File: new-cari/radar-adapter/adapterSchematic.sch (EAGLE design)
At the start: 25 parts, among them J3 JST-XH-03-PIN-LONG-PAD, J4 JST-XH-03-PIN-LONG-PAD, J5 AVR_SPI_PROG_3X2PTH, J6 UX60-MB-5S8, U1 ATMEGA32U4-AU, X1 TSX-3225 16.0000MF18X-AC0

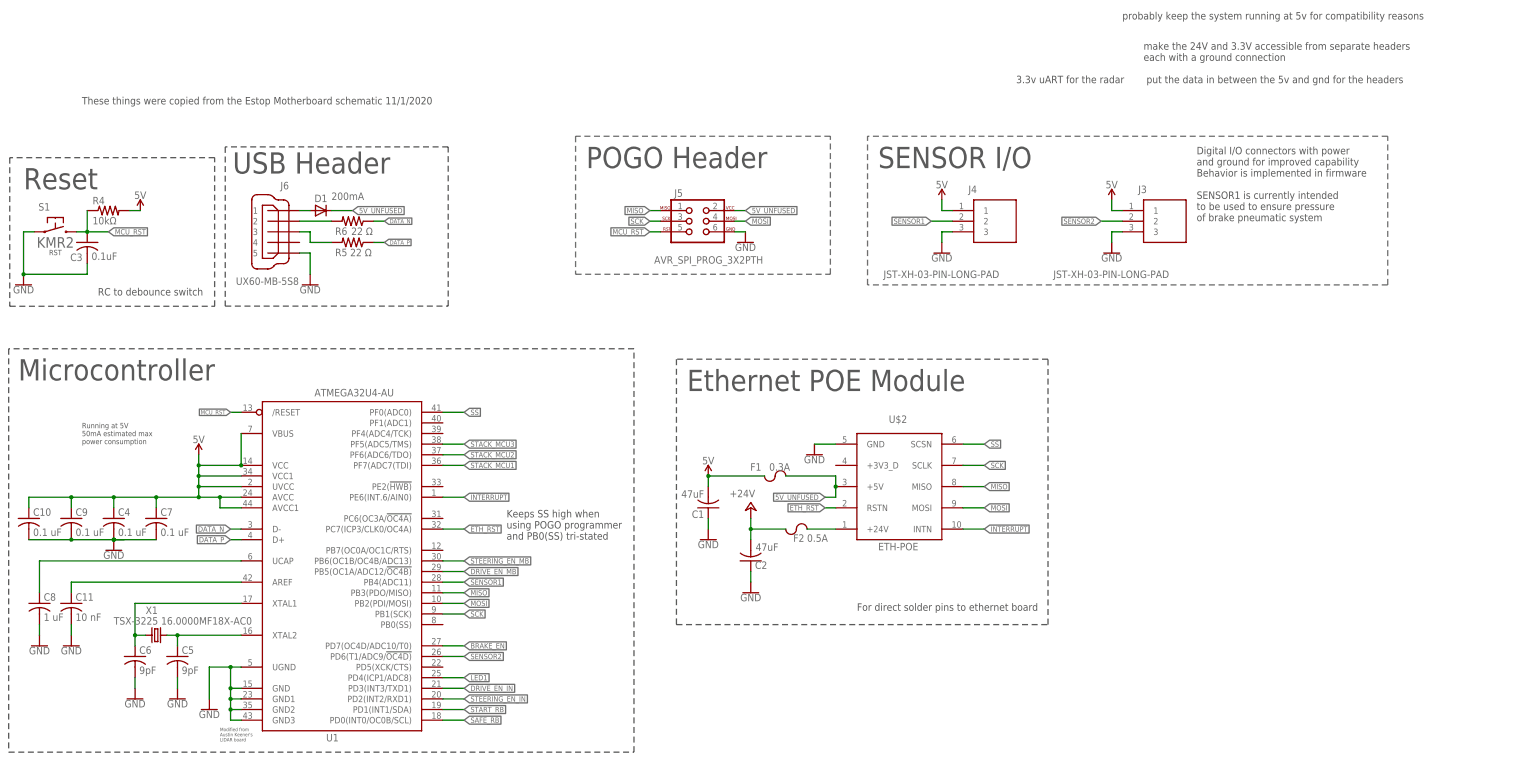
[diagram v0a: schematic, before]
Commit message: Added headers to board and rough board layout.
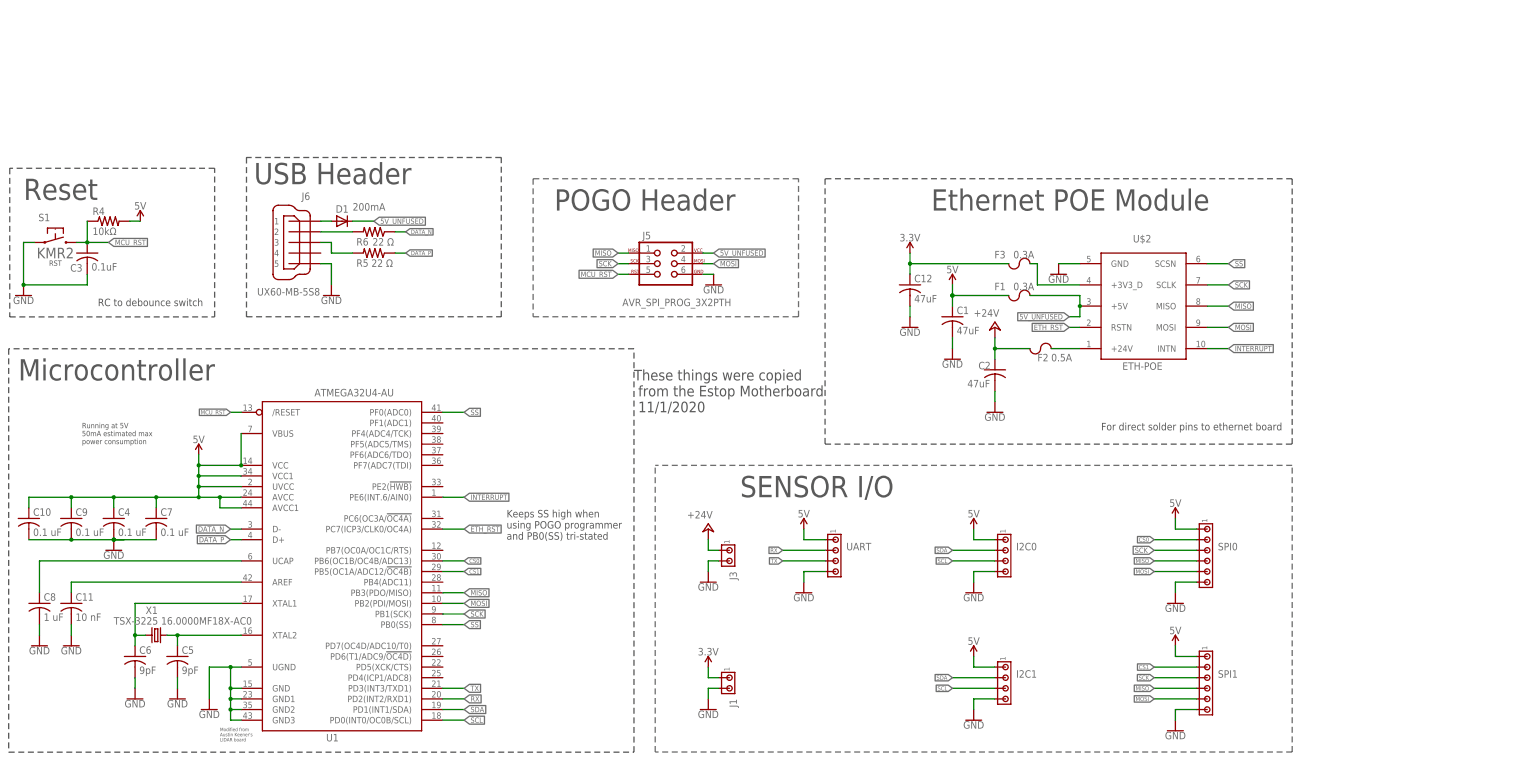
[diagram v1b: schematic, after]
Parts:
- removed J4: JST-XH-03-PIN-LONG-PAD, EVGP_Estop_Motherboard:JST-XH-03-PIN-LONG-PAD
- added C12: 47uF, rcl:C-USC1206
- added F3: 0.3A, RoboJackets-Fuses:CHIP_FUSE1206
- added I2C0, I2C1, UART: (no value), con-amp:MTA04-100
- added J1: (no value), con-amp:MTA02-100
- added SPI0, SPI1: (no value), con-amp:MTA06-100
- J3: value JST-XH-03-PIN-LONG-PAD -> (none); device EVGP_Estop_Motherboard:JST-XH-03-PIN-LONG-PAD -> con-amp:MTA02-100
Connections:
- removed net BRAKE_EN: U1.PD7(OC4D/ADC10/T0)
- removed net DRIVE_EN_IN: U1.PD3(INT3/TXD1)
- removed net DRIVE_EN_MB: U1.PB5(OC1A/ADC12/!OC4B)
- removed net LED1: U1.PD4(ICP1/ADC8)
- removed net SAFE_RB: U1.PD0(INT0/OC0B/SCL)
- removed net SENSOR1: J4.2, U1.PB4(ADC11)
- removed net SENSOR2: J3.2, U1.PD6(T1/ADC9/!OC4D)
- removed net STACK_MCU1: U1.PF7(ADC7(TDI)
- removed net STACK_MCU2: U1.PF6(ADC6/TDO)
- removed net STACK_MCU3: U1.PF5(ADC5/TMS)
- removed net START_RB: U1.PD1(INT1/SDA)
- removed net STEERING_EN_IN: U1.PD2(INT2/RXD1)
- removed net STEERING_EN_MB: U1.PB6(OC1B/OC4B/ADC13)
- new net 3.3V: C12.1, F3.1, J1.1
- new net CS0: SPI0.2, U1.PB6(OC1B/OC4B/ADC13)
- new net CS1: SPI1.2, U1.PB5(OC1A/ADC12/!OC4B)
- new net N$1: F3.2, U$2.+3V3_D
- new net N$3: U1.PB0(SS)
- new net RX: U1.PD2(INT2/RXD1), UART.2
- new net SCL: I2C0.3, I2C1.3, U1.PD0(INT0/OC0B/SCL)
- new net SDA: I2C0.2, I2C1.2, U1.PD1(INT1/SDA)
- new net TX: U1.PD3(INT3/TXD1), UART.3
- net +24V: now also C2.1, J3.1; no longer C2.2
- net 5V: now also C1.1, I2C0.1, I2C1.1, SPI0.1, SPI1.1, UART.1; no longer C1.2, J3.1, J4.1
- net GND: now also C1.2, C12.2, C2.2, I2C0.4, I2C1.4, J1.2, J3.2, SPI0.6, SPI1.6, UART.4; no longer C1.1, C2.1, J3.3, J4.3
- net MISO: now also SPI0.4, SPI1.4
- net MOSI: now also SPI0.5, SPI1.5
- net SCK: now also SPI0.3, SPI1.3
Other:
- note added: "These things were copied from the Estop Motherboard 11/1/2020"
- note removed: "3.3v uART for the radar"
- note removed: "Digital I/O connectors with power and ground for improved capability Behavior is implemented in firmware SENSOR1 is currently intended to be used to ensure pressure of brake pneumatic system"
- note removed: "These things were copied from the Estop Motherboard schematic 11/1/2020"
- note removed: "make the 24V and 3.3V accessible from separate headers each with a ground connection put the data in between the 5v and gnd for the headers"
- note removed: "probably keep the system running at 5v for compatibility reasons"
- moved on the sheet: C1, C2, C3, D1, F1, F2, J5, J6, R4, R5, R6, S1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

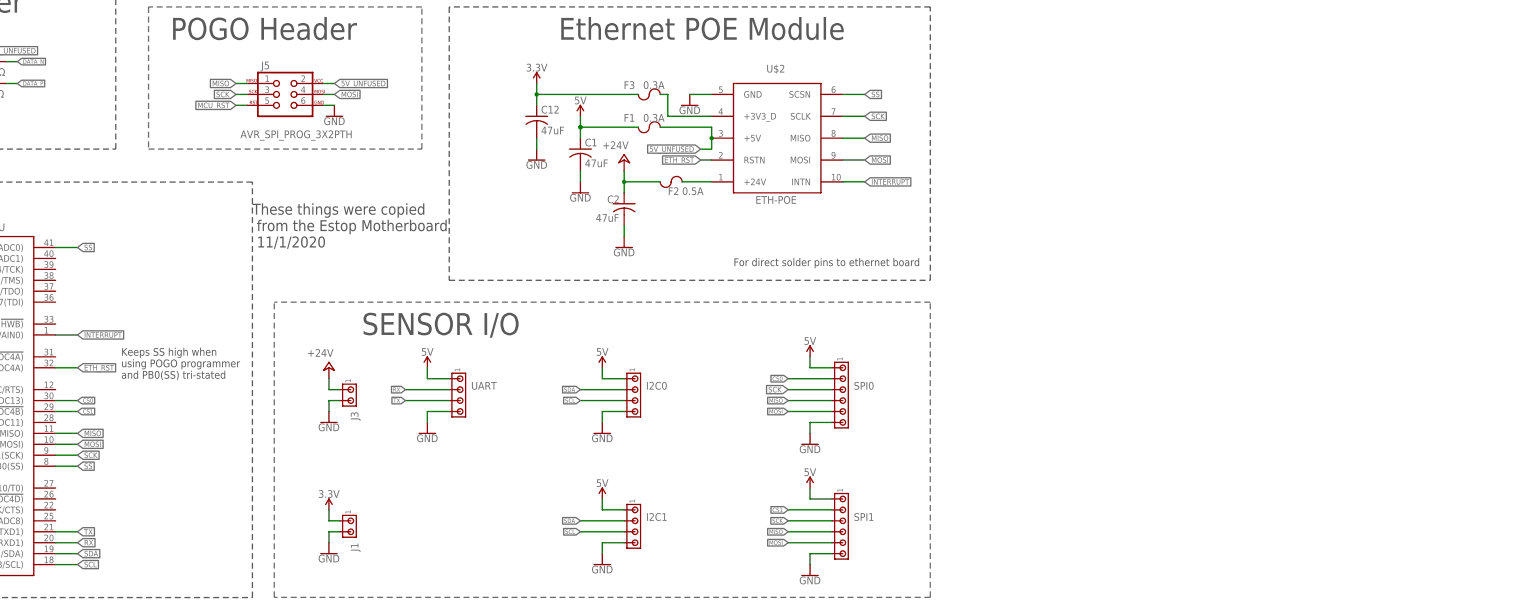
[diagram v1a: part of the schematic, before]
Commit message: Added bidirectional level shifters for 3.3v SPI and I2C connectivity
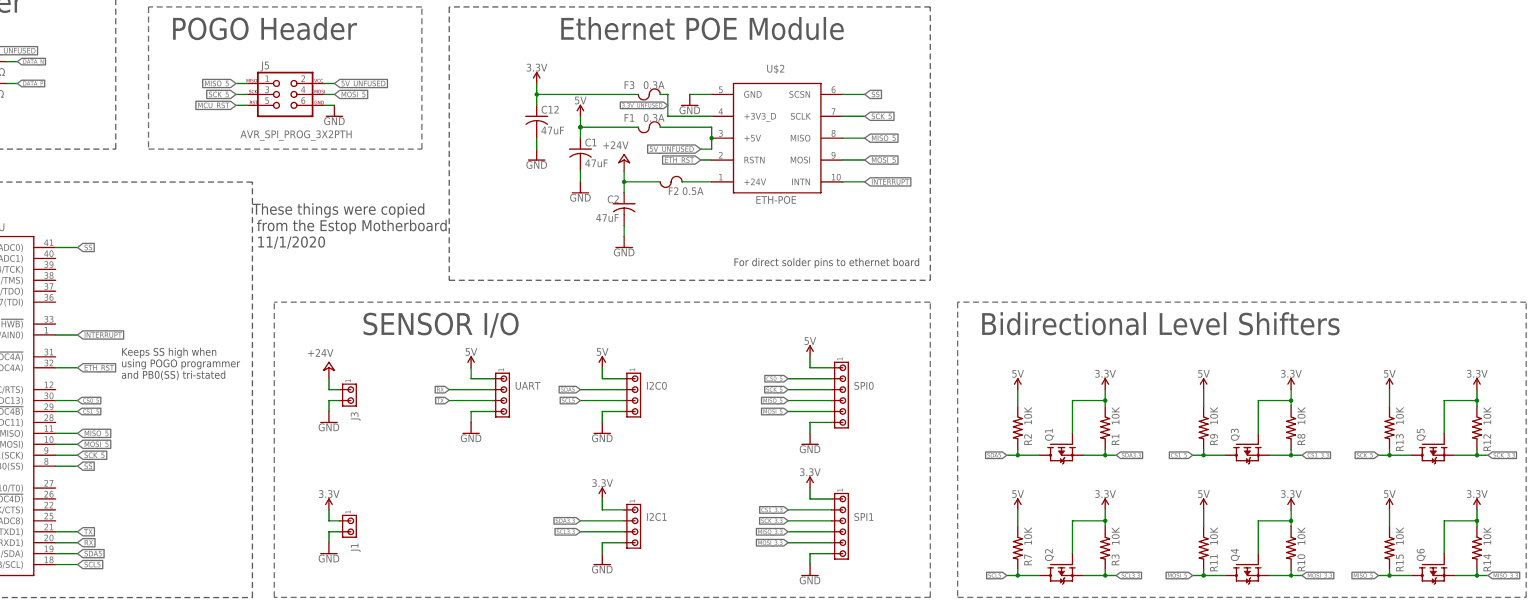
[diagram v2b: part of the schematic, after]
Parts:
- added Q1, Q2, Q3, Q4, Q5, Q6: BSA223SP, transistor-fet:BSA223SP
- added R1, R10, R11, R12, R13, R14, R15, R2, R3, R7, R8, R9: 10K, rcl:R-US_R0603
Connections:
- net CS0 renamed CS0_5
- net N$1 renamed 3.3V_UNFUSED
- removed net CS1: SPI1.2, U1.PB5(OC1A/ADC12/!OC4B)
- removed net MISO: J5.1, SPI0.4, SPI1.4, U$2.MISO, U1.PB3(PDO/MISO)
- removed net MOSI: J5.4, SPI0.5, SPI1.5, U$2.MOSI, U1.PB2(PDI/MOSI)
- removed net SCK: J5.3, SPI0.3, SPI1.3, U$2.SCLK, U1.PB1(SCK)
- removed net SCL: I2C0.3, I2C1.3, U1.PD0(INT0/OC0B/SCL)
- removed net SDA: I2C0.2, I2C1.2, U1.PD1(INT1/SDA)
- new net CS1_3.3: Q3.S, R8.2, SPI1.2
- new net CS1_5: Q3.D, R9.2, U1.PB5(OC1A/ADC12/!OC4B)
- new net MISO_3.3: Q6.S, R14.2, SPI1.4
- new net MISO_5: J5.1, Q6.D, R15.2, SPI0.4, U$2.MISO, U1.PB3(PDO/MISO)
- new net MOSI_3.3: Q4.S, R10.2, SPI1.5
- new net MOSI_5: J5.4, Q4.D, R11.2, SPI0.5, U$2.MOSI, U1.PB2(PDI/MOSI)
- new net SCK_3.3: Q5.S, R12.2, SPI1.3
- new net SCK_5: J5.3, Q5.D, R13.2, SPI0.3, U$2.SCLK, U1.PB1(SCK)
- new net SCL3.3: I2C1.3, Q2.S, R3.2
- new net SCL5: I2C0.3, Q2.D, R7.2, U1.PD0(INT0/OC0B/SCL)
- new net SDA3.3: I2C1.2, Q1.S, R1.2
- new net SDA5: I2C0.2, Q1.D, R2.2, U1.PD1(INT1/SDA)
- net 3.3V: now also I2C1.1, Q1.G, Q2.G, Q3.G, Q4.G, Q5.G, Q6.G, R1.1, R10.1, R12.1, R14.1, R3.1, R8.1, SPI1.1
- net 5V: now also R11.1, R13.1, R15.1, R2.1, R7.1, R9.1; no longer I2C1.1, SPI1.1
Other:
- note added: "Bidirectional Level Shifters"
- moved on the sheet: UART

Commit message: Copied sparkfun bidirectional level shifters. Added LEDs. Created switch device for UART voltage
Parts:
- removed C11: 10 nF, resistor:C-USC0603
- added LED1, LED3: RED, led:LEDCHIP-LED0603
- added LED2, LED4: GREEN, led:LEDCHIP-LED0603
- added Q7, Q8: BSS138, SparkFun:MOSFET-NCHANNELSMD
- added R16, R17, R18, R19: 10K, SparkFun:RESISTOR0603-RES
- added R24, R26: 330Ω, rcl:R-US_R0603
- added R25, R27: 220Ω, rcl:R-US_R0603
- added U$4: DPDT_SLIDE_SWITCH, DPDT-slide-switch:DPDT_SLIDE_SWITCH
- Q1, Q2, Q3, Q4, Q5, Q6: value BSA223SP -> BSS138; device transistor-fet:BSA223SP -> SparkFun:MOSFET-NCHANNELSMD
- R1, R10, R11, R12, R13, R14, R15, R2, R3, R7, R8, R9: device rcl:R-US_R0603 -> SparkFun:RESISTOR0603-RES
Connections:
- removed net AREF: C11.1, U1.AREF
- removed net SCL3.3: I2C1.3, Q2.S, R3.2
- removed net SCL5: I2C0.3, Q2.D, R7.2, U1.PD0(INT0/OC0B/SCL)
- removed net SDA3.3: I2C1.2, Q1.S, R1.2
- removed net SDA5: I2C0.2, Q1.D, R2.2, U1.PD1(INT1/SDA)
- new net LED3: R26.2, U$4.P4
- new net LED4: R27.2, U$4.P6
- new net N$1: LED1.C, R24.2
- new net N$4: LED3.A, R26.1
- new net N$6: LED2.C, R25.2
- new net N$8: LED4.A, R27.1
- new net RX_LVL: Q4.S, R10.2, UART.2
- new net SCL_3.3: I2C1.3, Q1.S, R1.2
- new net SCL_5: I2C0.3, Q1.D, R2.2, U1.PD0(INT0/OC0B/SCL)
- new net SDA_3.3: I2C1.2, Q2.S, R3.2
- new net SDA_5: I2C0.2, Q2.D, R7.2, U1.PD1(INT1/SDA)
- new net TX_LVL: Q3.S, R8.2, UART.3
- new net UART_LVL: Q3.G, Q4.G, R10.1, R8.1, U$4.P2
- net 3.3V: now also LED2.A, Q7.G, Q8.G, R16.1, R18.1, U$4.P3; no longer Q3.G, Q4.G, R10.1, R8.1
- net 5V: now also LED1.A, R17.1, R19.1, U$4.P1, U$4.P5
- net CS1_3.3: now also Q8.S, R18.2; no longer Q3.S, R8.2
- net CS1_5: now also Q8.D, R19.2; no longer Q3.D, R9.2
- net GND: now also LED3.C, LED4.C, R24.1, R25.1; no longer C11.2
- net MOSI_3.3: now also Q5.S, R12.2; no longer Q4.S, R10.2
- net MOSI_5: now also Q5.D, R13.2; no longer Q4.D, R11.2
- net RX: now also Q4.D, R11.2; no longer UART.2
- net SCK_3.3: now also Q7.S, R16.2; no longer Q5.S, R12.2
- net SCK_5: now also Q7.D, R17.2; no longer Q5.D, R13.2
- net TX: now also Q3.D, R9.2; no longer UART.3
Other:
- note added: "I2C"
- note added: "LEDs"
- note added: "Power indicators and UART level indicators"
- note added: "SPI"
- note added: "UART"
- moved on the sheet: R1, R10, R11, R12, R13, R14, R15, R2, R3, R7, R8, R9

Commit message: Routed all the traces
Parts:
- removed LED2: GREEN, led:LEDCHIP-LED0603
- removed R25: 220Ω, rcl:R-US_R0603
- renumbered I2C0 to I2C_5V, I2C1 to I2C_3.3V, J1 to 3.3V, J3 to 24V, SPI0 to SPI_5V, SPI1 to SPI_3.3V
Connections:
- removed net N$6: LED2.C, R25.2
- net 3.3V: no longer LED2.A
- net 5V: no longer UART.1
- net CS0_5: now also U1.PF1(ADC1); no longer U1.PB6(OC1B/OC4B/ADC13)
- net CS1_5: now also U1.PF4(ADC4/TCK); no longer U1.PB5(OC1A/ADC12/!OC4B)
- net GND: no longer R25.1
- net UART_LVL: now also UART.1

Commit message: Fixed Silkscreen, added header pinout, misc touchups
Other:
- note added: "Power indicator and UART level indicators"
- note added: "S2"
- note removed: "Power indicators and UART level indicators"

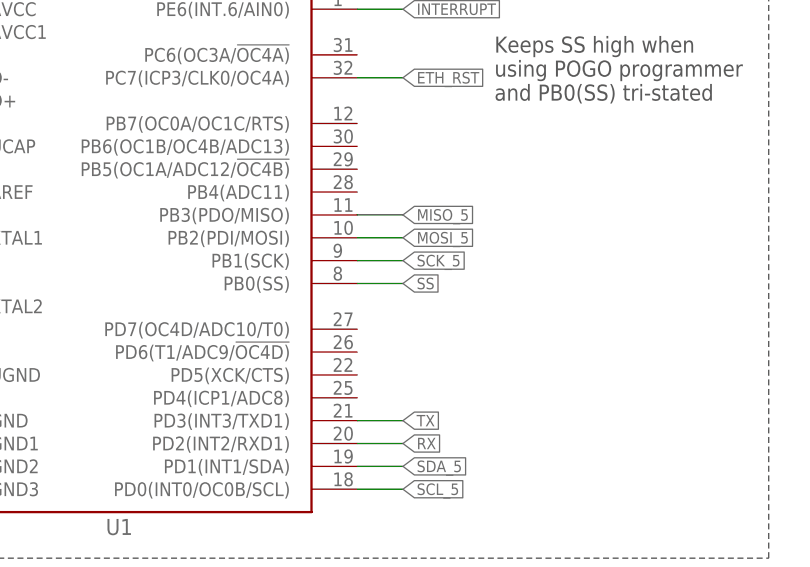
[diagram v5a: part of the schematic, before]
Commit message: began some DR fixes
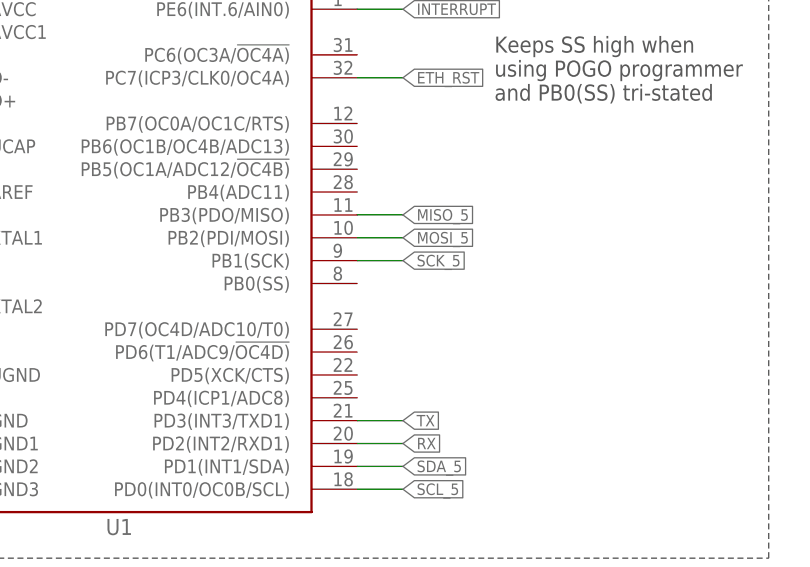
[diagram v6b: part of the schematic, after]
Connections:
- removed net N$3: U1.PB0(SS)
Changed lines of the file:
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@@
 <?xml version="1.0" encoding="utf-8"?>
 <!DOCTYPE eagle SYSTEM "eagle.dtd">
-<eagle version="9.6.2">
+<eagle version="9.5.1">
 <drawing>
 <settings>
@@
 <label x="302.26" y="149.86" size="1.27" layer="95" font="vector" xref="yes"/>
 </segment>
-<segment>
-<label x="119.38" y="63.5" size="1.27" layer="95" font="vector" xref="yes"/>
-</segment>
 </net>
 <net name="ETH_RST" class="0">
@@
 </segment>
 </net>
-<net name="N$3" class="0">
-<segment>
-<pinref part="U1" gate="G$1" pin="PB0(SS)"/>
-<wire x1="114.3" y1="63.5" x2="119.38" y2="63.5" width="0.1524" layer="91"/>
-</segment>
-</net>

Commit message: added levelshifter link
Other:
- note added: "https://www.nxp.com/docs/en/application-note/AN10441.pdf"
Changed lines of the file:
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@@
 <?xml version="1.0" encoding="utf-8"?>
 <!DOCTYPE eagle SYSTEM "eagle.dtd">
-<eagle version="9.5.1">
+<eagle version="9.5.0">
 <drawing>
 <settings>
@@
 <wire x1="373.38" y1="106.68" x2="322.58" y2="106.68" width="0.1524" layer="97" style="shortdash"/>
 <text x="444.5" y="63.5" size="1.778" layer="95">S2</text>
+<text x="414.02" y="96.52" size="1.778" layer="91">https://www.nxp.com/docs/en/application-note/AN10441.pdf</text>
 </plain>
 <instances>
